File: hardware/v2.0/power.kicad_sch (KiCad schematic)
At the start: 48 parts, among them U1 ECP5U-25F-CABGA256, U2 TLV62569DBV, U3 TLV62569DBV, U4 TLV62569DBV

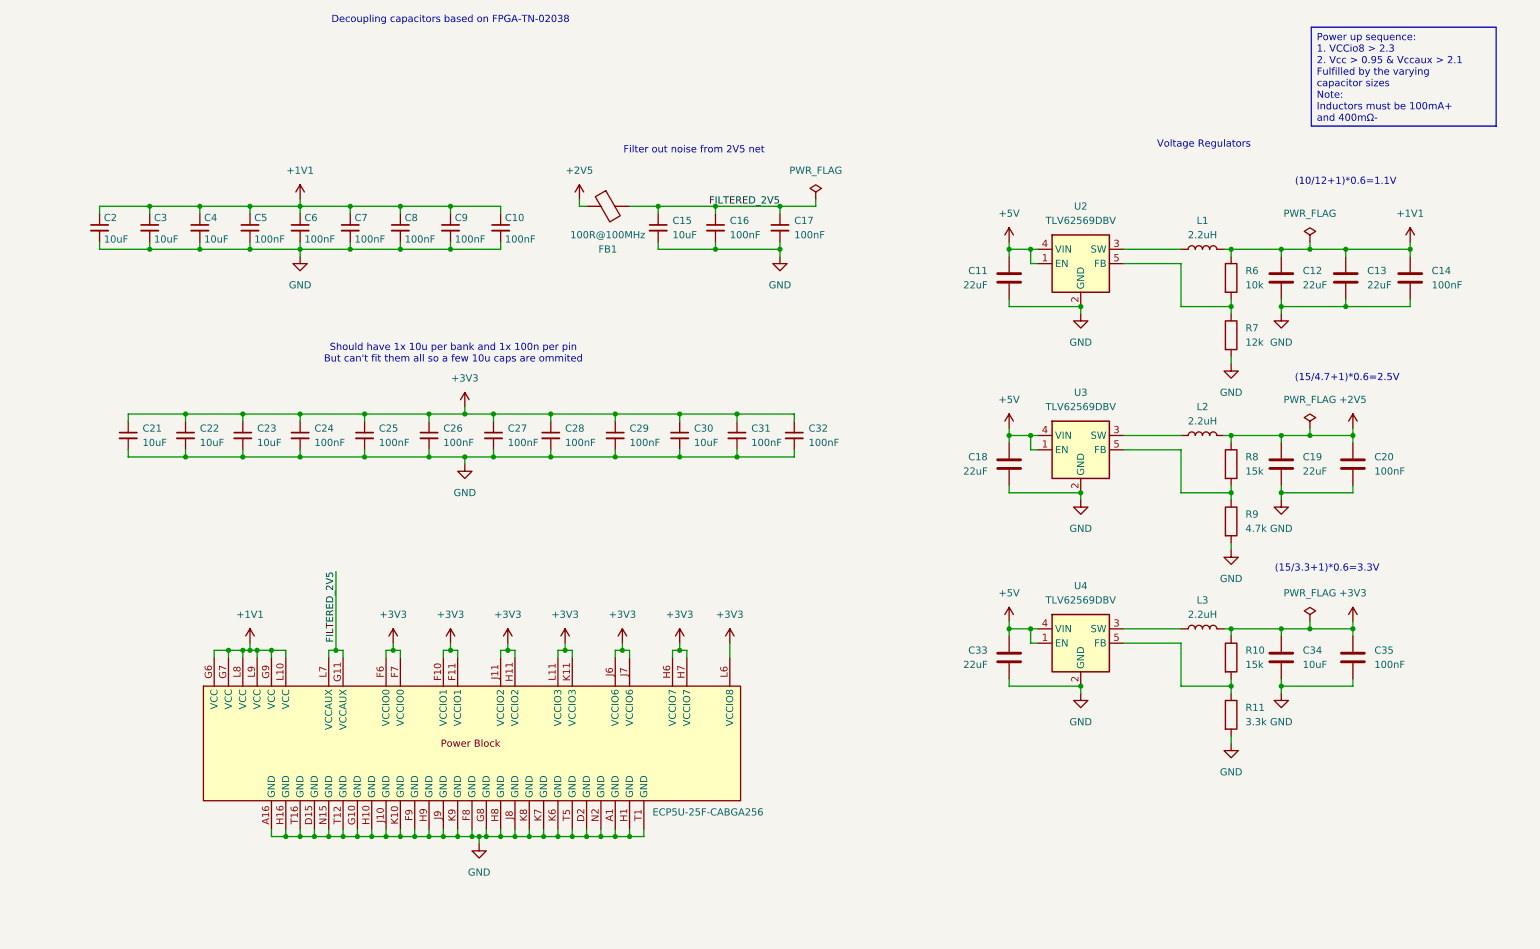
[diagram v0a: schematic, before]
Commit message: Replaced 2.5 and 1.1V regulators with single LTC3407A-2
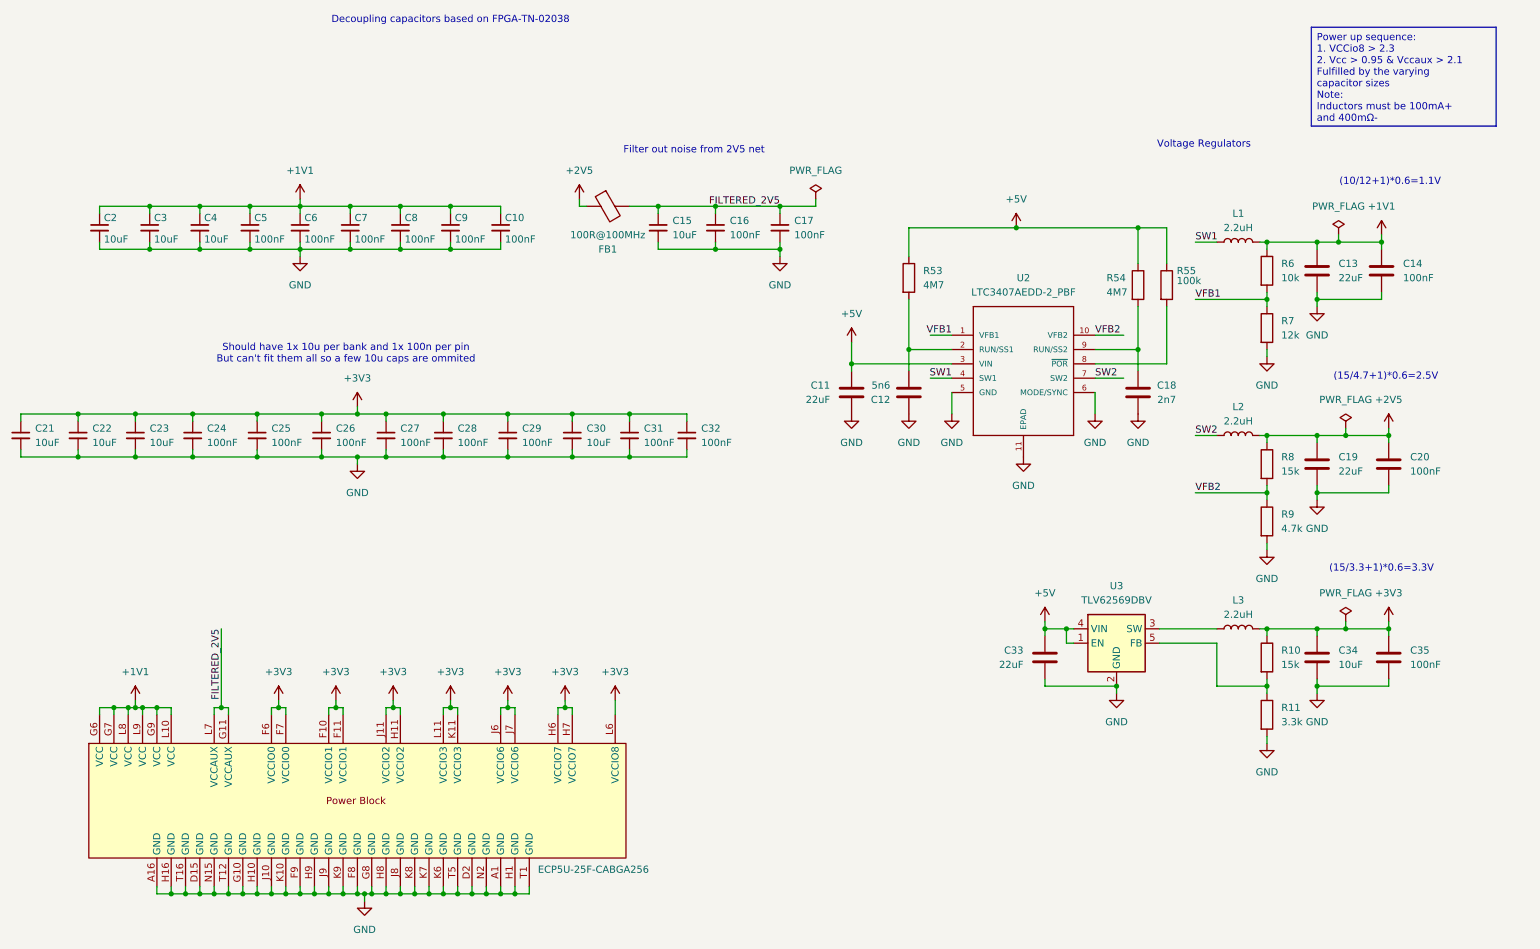
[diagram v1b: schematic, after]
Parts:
- removed U2, U3: TLV62569DBV, Package_TO_SOT_SMD:SOT-23-5, symbol Regulator_Switching:TLV62569DBV
- added R53, R54: 4M7, Resistor_SMD:R_0402_1005Metric, symbol Device:R
- added R55: 100k, Resistor_SMD:R_0402_1005Metric, symbol Device:R
- added U2: LTC3407AEDD-2_PBF, LTC3407AEDD-2_PBF:DFN-10_DD, symbol LTC3407AEDD-2_PBF:LTC3407AEDD-2_PBF
- C12: value 22uF -> 5n6; footprint Capacitor_SMD:C_0603_1608Metric -> Capacitor_SMD:C_0402_1005Metric; LCSC Link https://lcsc.com/product-detail/Multilayer-Ceramic-Capacito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 -> https://www.lcsc.com/product-detail/C307435.html; LCSC Part # C59461 -> C307435; Manufactuer Part Number CL10A226MQ8NRNC -> CL05B562KB5NNNC
- C18: value 22uF -> 2n7; footprint Capacitor_SMD:C_0603_1608Metric -> Capacitor_SMD:C_0402_1005Metric; LCSC Link https://lcsc.com/product-detail/Multilayer-Ceramic-Capacito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 -> https://www.lcsc.com/product-detail/C84704.html; LCSC Part # C59461 -> C84704; Manufactuer Part Number CL10A226MQ8NRNC -> CL05B272KB5NNNC
- renumbered U4 to U3
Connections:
- net +1V1: no longer C12.1
- net +5V: now also R53.1, R54.1, R55.1, U2.3 (VIN); no longer C18.1
- net GND: now also C12.1, U2.11 (EPAD), U2.5 (GND), U2.6 (MODE/SYNC); no longer C12.2
- net VFB1: now reaches R6.2, R7.1
- net VFB1: now also U2.1 (VFB1)
- net SW1: now reaches L1.1
- net SW1: now also U2.4 (SW1)
- net SW2: now reaches L2.1
- net SW2: now also U2.7 (SW2)
- net VFB2: now reaches R8.2, R9.1
- net VFB2: now also U2.10 (VFB2)
- new net: C12.2, R53.2, U2.2 (RUN/SS1)
- new net: C18.1, R54.2, U2.9 (RUN/SS2)
- new net: R55.2, U2.8 (~{POR})
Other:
- moved on the sheet: C11, C13, C14, C19, C20, C21, C22, C23, C24, C25, C26, C27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

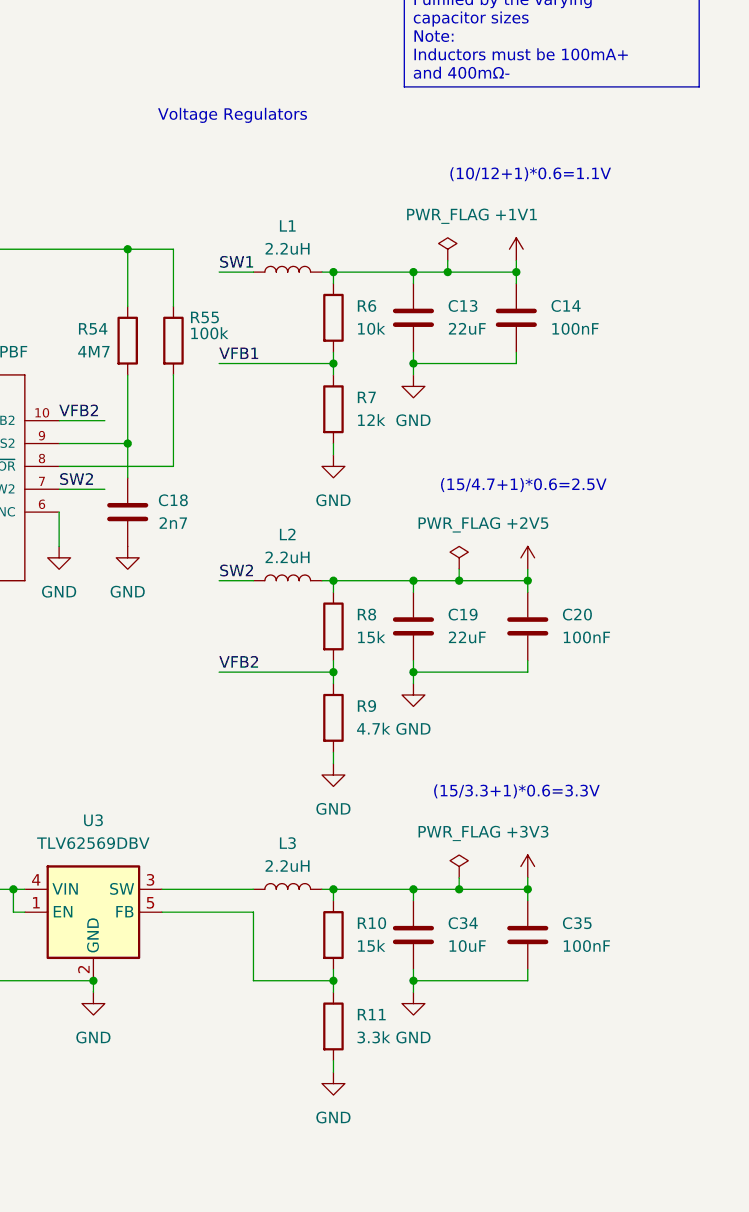
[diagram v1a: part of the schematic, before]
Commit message: LDOs dividers update
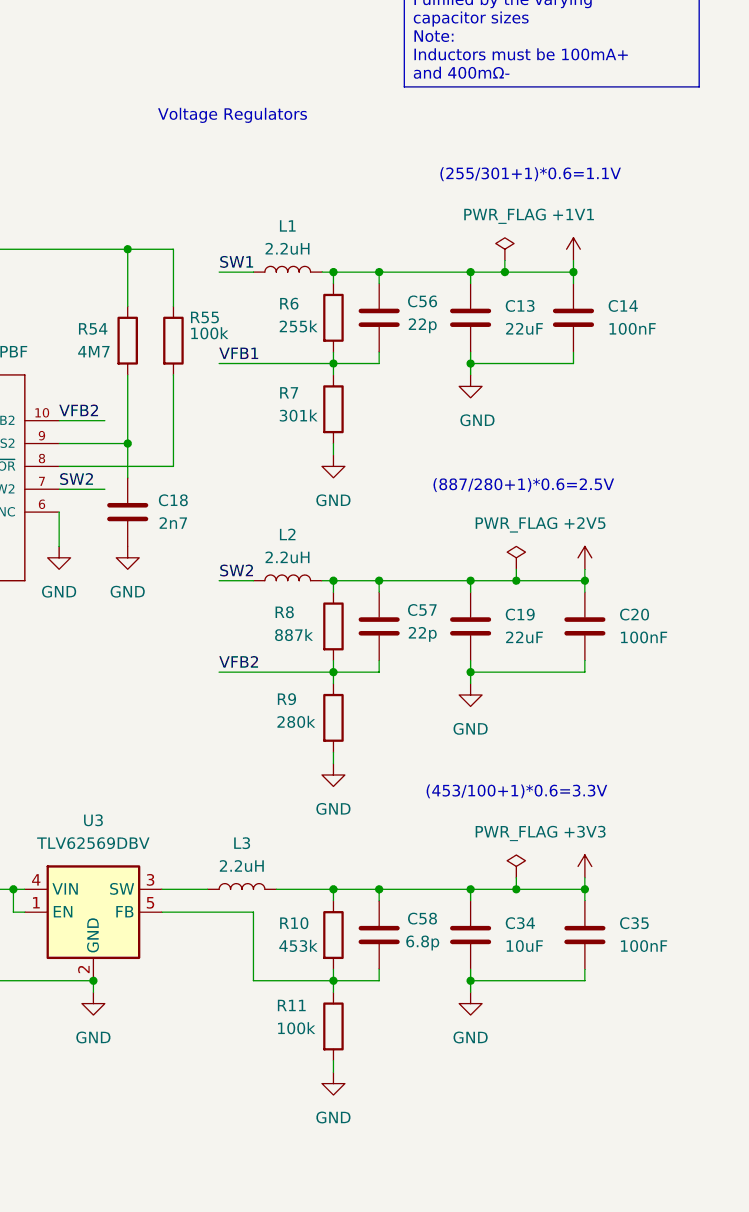
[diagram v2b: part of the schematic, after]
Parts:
- added C56, C57: 22p, Capacitor_SMD:C_0402_1005Metric, symbol Device:C
- added C58: 6.8p, Capacitor_SMD:C_0402_1005Metric, symbol Device:C
- R10: value 15k -> 453k; LCSC Link https://lcsc.com/product-detail/Chip-Resistor-Surface-Mount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 -> https://www.lcsc.com/product-detail/C27009.html; LCSC Part # C25756 -> C27009; Manufactuer Part Number 0402WGF1502TCE -> 0402WGF4533TCE
- R11: value 3.3k -> 100k; LCSC Link https://lcsc.com/product-detail/Chip-Resistor-Surface-Mount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 -> https://www.lcsc.com/product-detail/C25741.html; LCSC Part # C25890 -> C25741; Manufactuer Part Number 0402WGF3301TCE -> 0402WGF1003TCE
- R6: value 10k -> 255k; LCSC Link https://lcsc.com/product-detail/Chip-Resistor-Surface-Mount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 -> https://www.lcsc.com/product-detail/C270623.html; LCSC Part # C25744 -> C270623; Manufactuer Part Number 0402WGF1002TCE -> 0402WGF2553TCE
- R7: value 12k -> 301k; LCSC Link https://lcsc.com/product-detail/Chip-Resistor-Surface-Mount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 -> https://www.lcsc.com/product-detail/C25775.html; LCSC Part # C25752 -> C25775; Manufactuer Part Number 0402WGF1202TCE -> 0402WGF3013TCE
- R8: value 15k -> 887k; LCSC Link https://lcsc.com/product-detail/Chip-Resistor-Surface-Mount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 -> https://www.lcsc.com/product-detail/C423127.html; LCSC Part # C25756 -> C423127; Manufactuer Part Number 0402WGF1502TCE -> 0402WGF8873TCE
- R9: value 4.7k -> 280k; LCSC Link https://lcsc.com/product-detail/Chip-Resistor-Surface-Mount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 -> https://www.lcsc.com/product-detail/C46006.html; LCSC Part # C25900 -> C46006; Manufactuer Part Number 0402WGF4701TCE -> 0402WGF2803TCE
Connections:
- net +1V1: now also C56.1
- net +2V5: now also C57.1
- net +3V3: now also C58.1
- net VFB1: now also C56.2
- net VFB2: now also C57.2
- net at R10.2, R11.1, U3.5 (FB): now also C58.2
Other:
- note added: "(255/301+1)*0.6=1.1V"
- note added: "(453/100+1)*0.6=3.3V"
- note added: "(887/280+1)*0.6=2.5V"
- note removed: "(10/12+1)*0.6=1.1V"
- note removed: "(15/3.3+1)*0.6=3.3V"
- note removed: "(15/4.7+1)*0.6=2.5V"
- moved on the sheet: C13, C14, C19, C20, C34, C35, L3

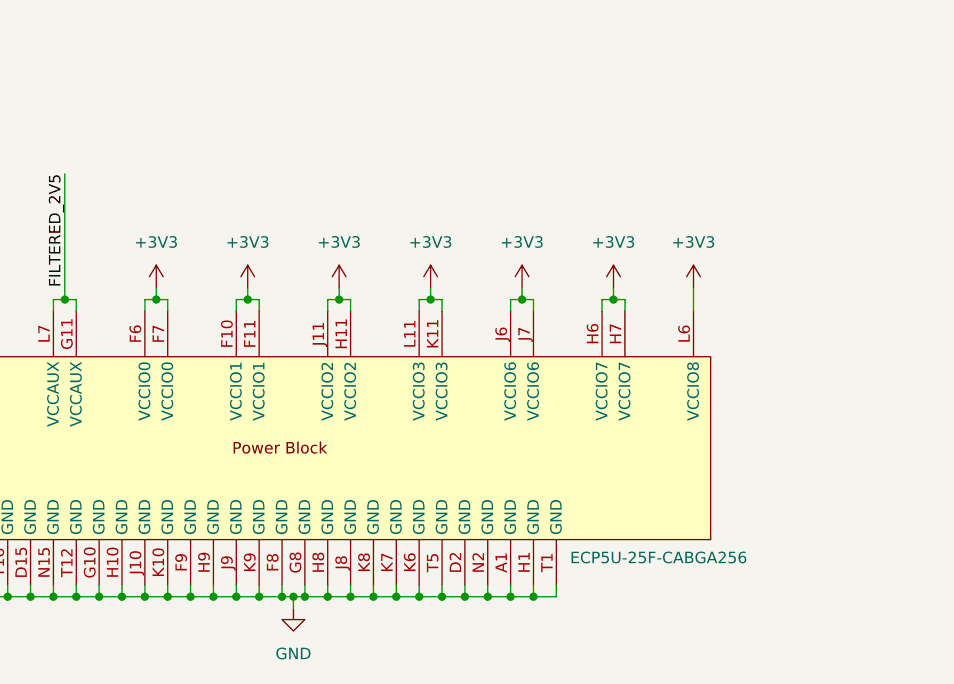
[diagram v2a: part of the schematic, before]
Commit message: ADC 6 diff lines
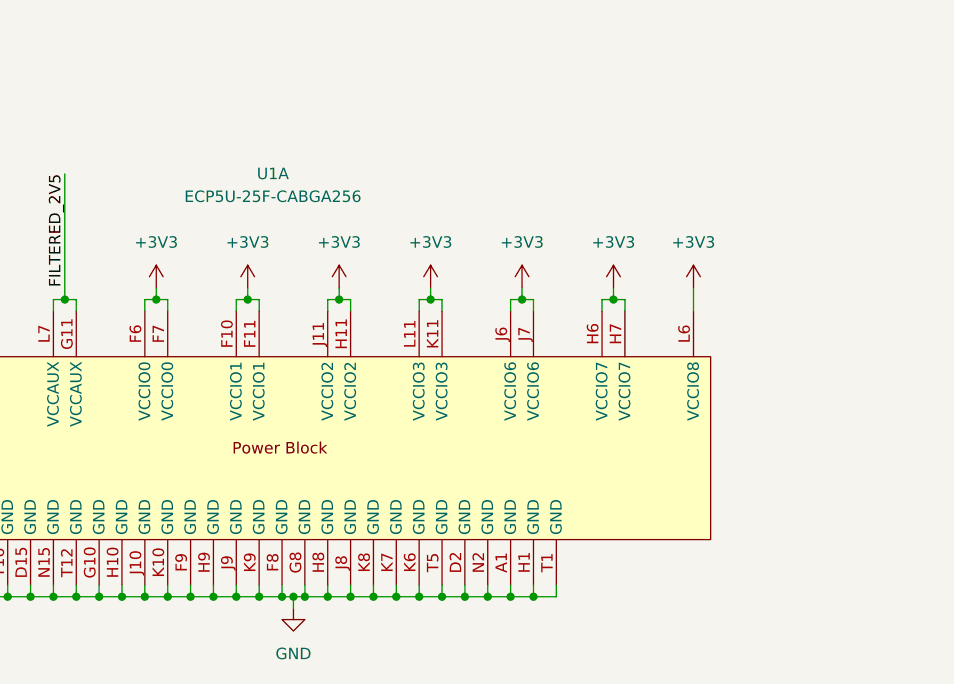
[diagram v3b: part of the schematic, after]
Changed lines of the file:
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@@
 		(dnp no)
 		(property "Reference" "U1"
-			(at 78.232 84.582 0)
+			(at 78.994 121.92 0)
 			(effects
 				(font
 					(size 1.27 1.27)
 				)
-				(hide yes)
 			)
 		)
 		(property "Value" "ECP5U-25F-CABGA256"
-			(at 112.014 164.592 0)
+			(at 78.994 124.46 0)
 			(effects
 				(font
 					(size 1.27 1.27)
 				)
-				(justify left)
 			)
 		)
@@
 					(reference "U1")
 					(unit 1)
+				)
+				(path "/f88da08e-cf42-4d03-a08f-3f602fe6658d/b5a9aa02-311b-4a9a-a7d4-646f15cdd9c2"
+					(reference "U1")
+					(unit 1)

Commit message: ADC CLKOUT±
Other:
- company: Chengyin Yao (cheyao), Vadym Vikulin -> Vadym Vikulin, Chengyin Yao (cheyao)
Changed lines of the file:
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@@
 	(title_block
 		(title "Icepi Zero")
-		(date "2026-01-05")
-		(rev "v2.0")
-		(company "Chengyin Yao (cheyao), Vadym Vikulin")
-		(comment 1 "https://github.com/cheyao/icepi-zero")
+		(date "2026-01-17")
+		(rev "v2.1")
+		(company "Vadym Vikulin, Chengyin Yao (cheyao)")
+		(comment 1 "https://github.com/vikulin/icepi-zero")
 		(comment 2 "License: Solderpad")
 		(comment 9 "OSHWA FR000026")
@@
 		(pin "P11"
 		)
+		(pin "N6"
+		)
 		(instances

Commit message: ADC power
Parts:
- added C62, C63: 10uF, Capacitor_SMD:C_0603_1608Metric, symbol Device:C
- added U4: LP5912-1.8DRV, Package_SON:WSON-6-1EP_2x2mm_P0.65mm_EP1x1.6mm_ThermalVias, symbol Regulator_Linear:LP5912-1.8DRV
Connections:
- net +3V3: now also C62.1, U4.4 (EN), U4.6 (IN)
- net GND: now also C62.2, C63.2, U4.3 (PG), U4.5 (GND), U4.7 (EP)
- new net +1V8: C63.1, U4.1 (OUT)
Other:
- moved on the sheet: C13, C14, C19, C20, C33, C34, C35, C56, C57, C58, L1, L2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

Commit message: ADC power
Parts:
- added C64: 10uF, Capacitor_SMD:C_0603_1608Metric, symbol Device:C
- added C65: 1u, Capacitor_SMD:C_0402_1005Metric, symbol Device:C
- added C66: 100n, Capacitor_SMD:C_0402_1005Metric, symbol Device:C
- added FB2: 1k@100MHz, Inductor_SMD:L_0603_1608Metric, symbol Device:FerriteBead
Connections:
- net +1V8: now also C64.1, FB2.1
- net GND: now also C64.2, C65.2, C66.1
- new net FILTERED_1V8: C65.1, C66.2, FB2.2
